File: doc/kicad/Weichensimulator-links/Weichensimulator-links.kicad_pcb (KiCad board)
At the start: 2 copper layers, 38.1 x 38.1 mm, 9 parts, among them J1 Conn_01x02_Male, J2 Power, J3 Conn_01x02_Male, K1 HFD2_005-S-L2-D

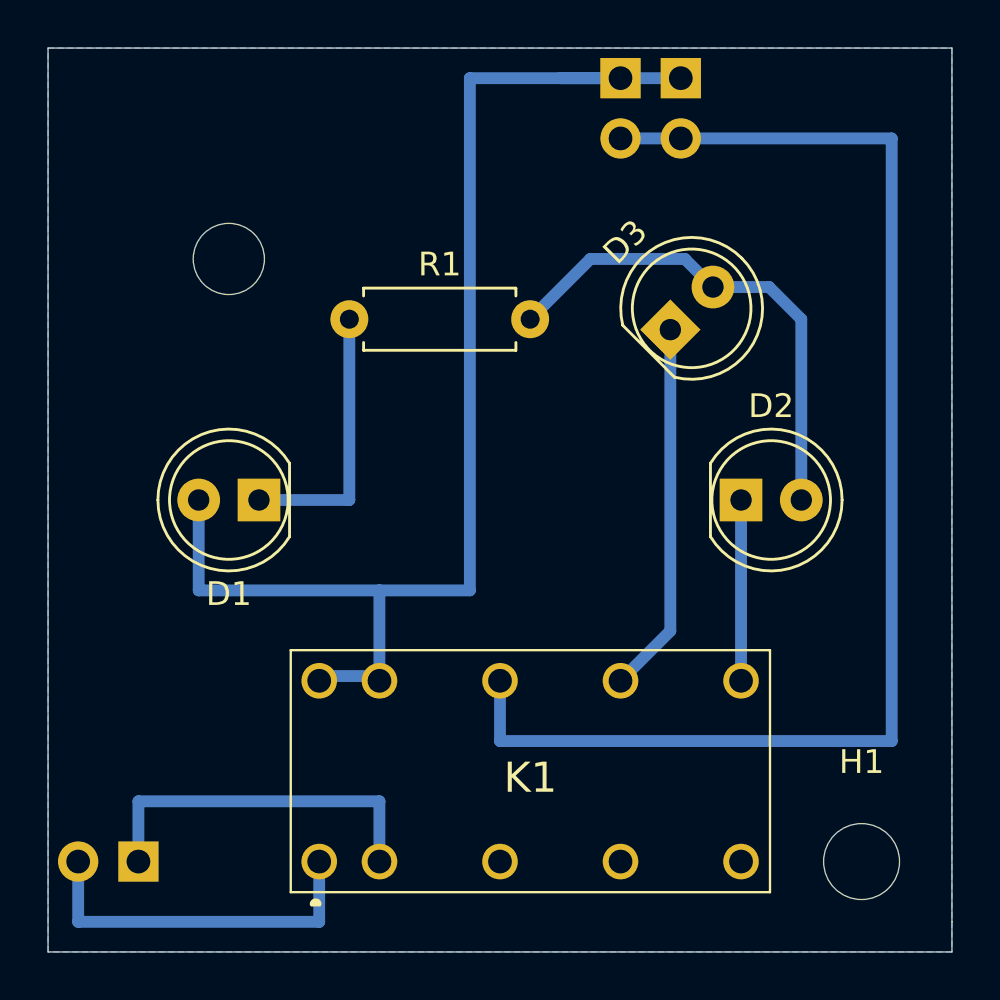
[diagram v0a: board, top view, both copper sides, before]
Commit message: Ecken rund gemacht, alle mit Montagelöcher
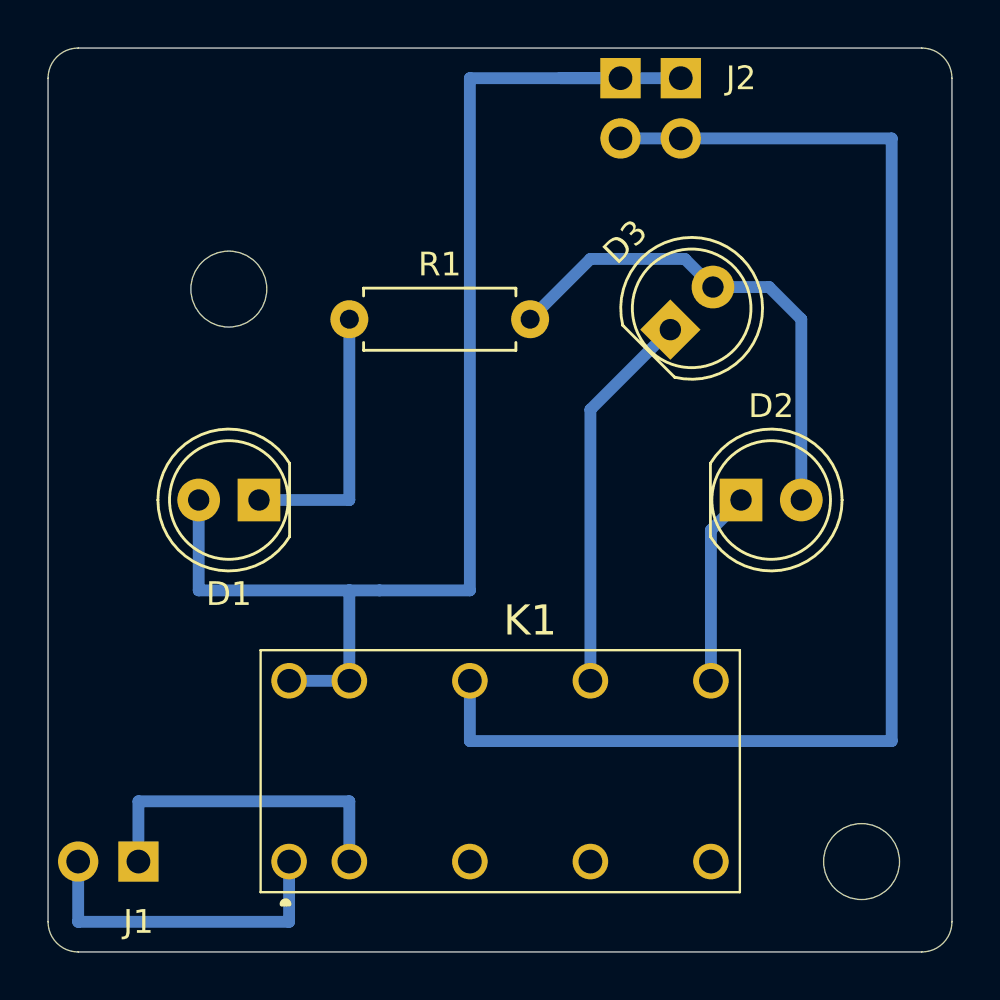
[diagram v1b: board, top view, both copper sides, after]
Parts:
- added H1: MountingHole, Mounting_Holes:MountingHole_3.2mm_M3, F.Cu at (123.2, 97.8)
- moved K1 1.27 mm to (125.7, 121.9)
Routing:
- net Net-(J1-Pad2): track 15.4 -> 14.0 mm
- net GND: track 55.9 -> 57.2 mm
- net Net-(J1-Pad1): track 15.0 -> 14.0 mm
- net Net-(D2-Pad1): track 7.42 -> 8.15 mm
- net Net-(D3-Pad1): track 15.7 -> 16.2 mm
- removed copper zone on B.Cu, net GND
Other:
- outline, holes or cut-outs redrawn
- board text added: "+5V"
- board text added: "GND"
- board text added: "©H3-H5N6 2021 Weiche li v1.0"

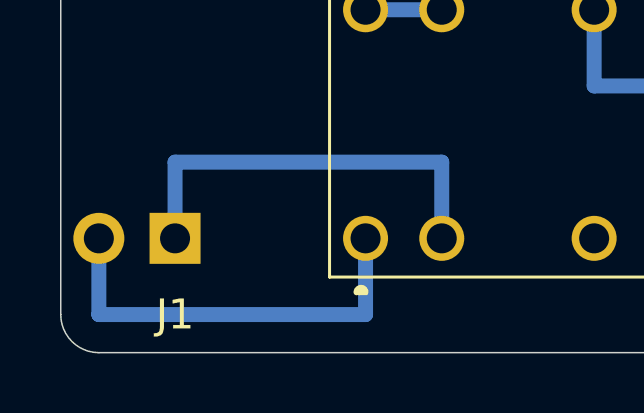
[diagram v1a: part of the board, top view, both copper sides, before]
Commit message: Platinen, die an jlcpcb geschickt worden sind.
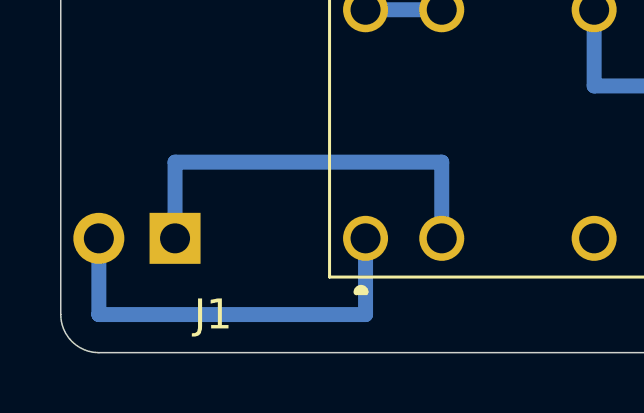
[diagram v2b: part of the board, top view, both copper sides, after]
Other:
- board text added: "A"
- board text added: "G"

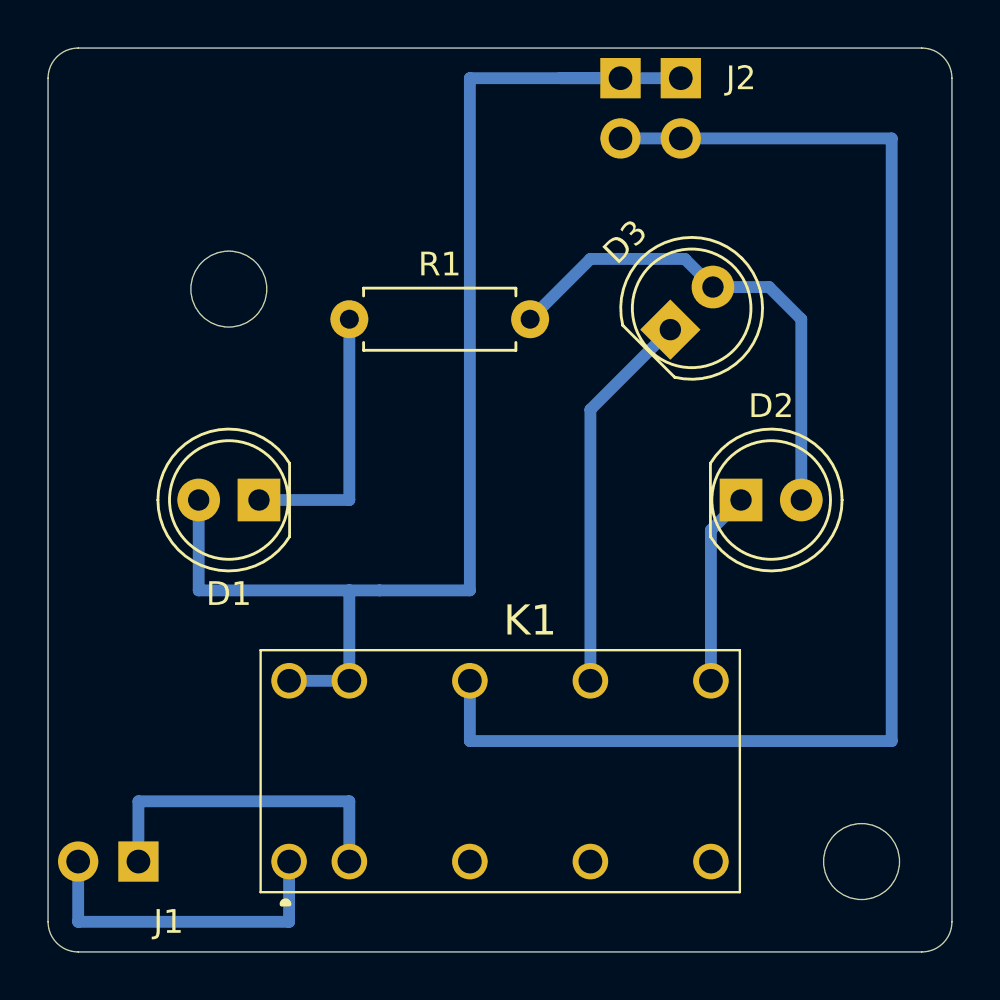
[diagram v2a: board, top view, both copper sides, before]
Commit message: beschreibung auf Bestückungssete, 90°-Kurven durch 45° erstetzt
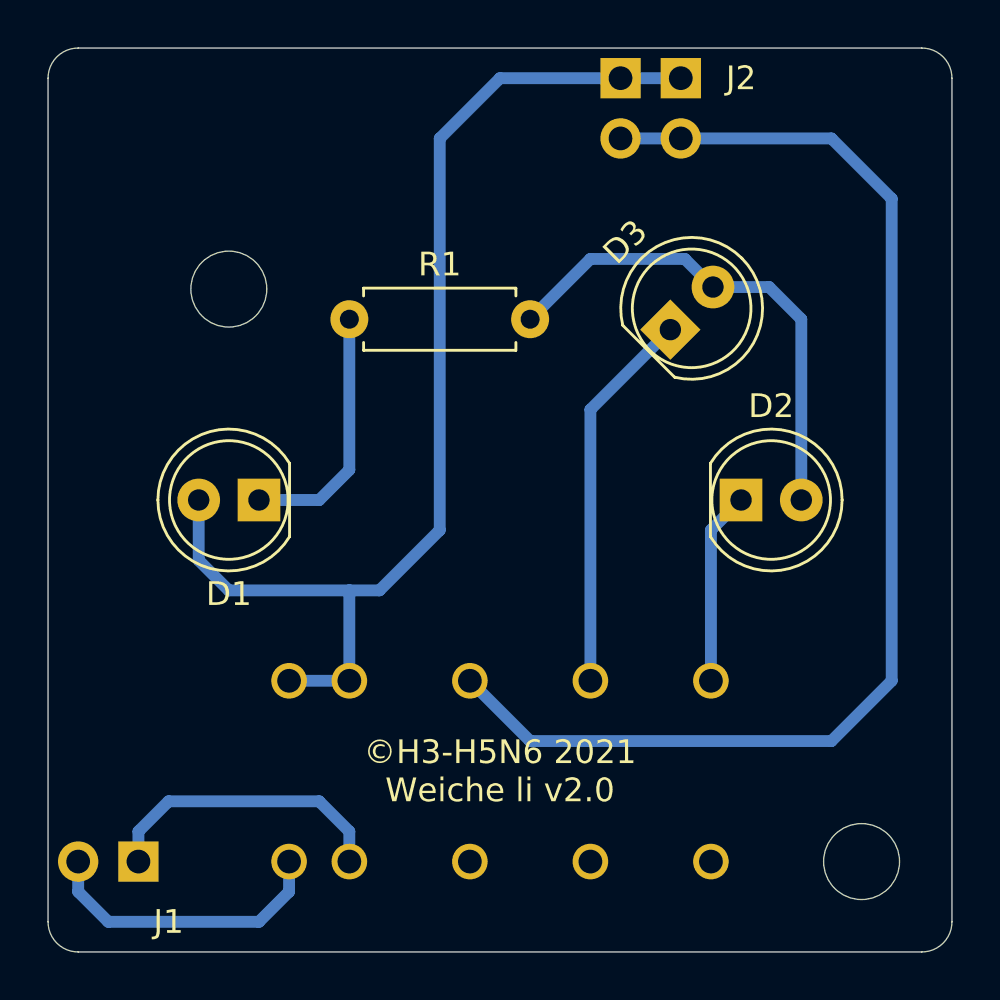
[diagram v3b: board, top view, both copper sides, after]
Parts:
- K1: moved to B.Cu
- moved K1 7.62 mm to (125.7, 114.3)
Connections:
- K1 pad 1: Net-(J1-Pad2) -> +5V
- K1 pad 11: Net-(D3-Pad1) -> (no net)
- K1 pad 13: GND -> (no net)
- K1 pad 15: +5V -> Net-(J1-Pad1)
- K1 pad 16: +5V -> Net-(J1-Pad2)
- K1 pad 2: Net-(J1-Pad1) -> +5V
- K1 pad 4: (no net) -> GND
- K1 pad 6: (no net) -> Net-(D3-Pad1)
- K1 pad 8: (no net) -> Net-(D2-Pad1)
- K1 pad 9: Net-(D2-Pad1) -> (no net)
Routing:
- net +5V: track 54.6 -> 48.4 mm
- net GND: track 57.2 -> 52.7 mm
- net Net-(J1-Pad1): track 14.0 -> 12.5 mm
- net Net-(J1-Pad2): track 14.0 -> 12.5 mm
- net Net-(D1-Pad1): track 11.4 -> 10.7 mm
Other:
- board text added: "©H3-H5N6 2021 Weiche li v2.0"
- board text removed: "©H3-H5N6 2021 Weiche li v1.0"

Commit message: Dateien aufgeräumt
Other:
- net class Default removed
